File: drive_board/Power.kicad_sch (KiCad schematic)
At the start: 9 parts, among them J1 Molex_Megafit_02

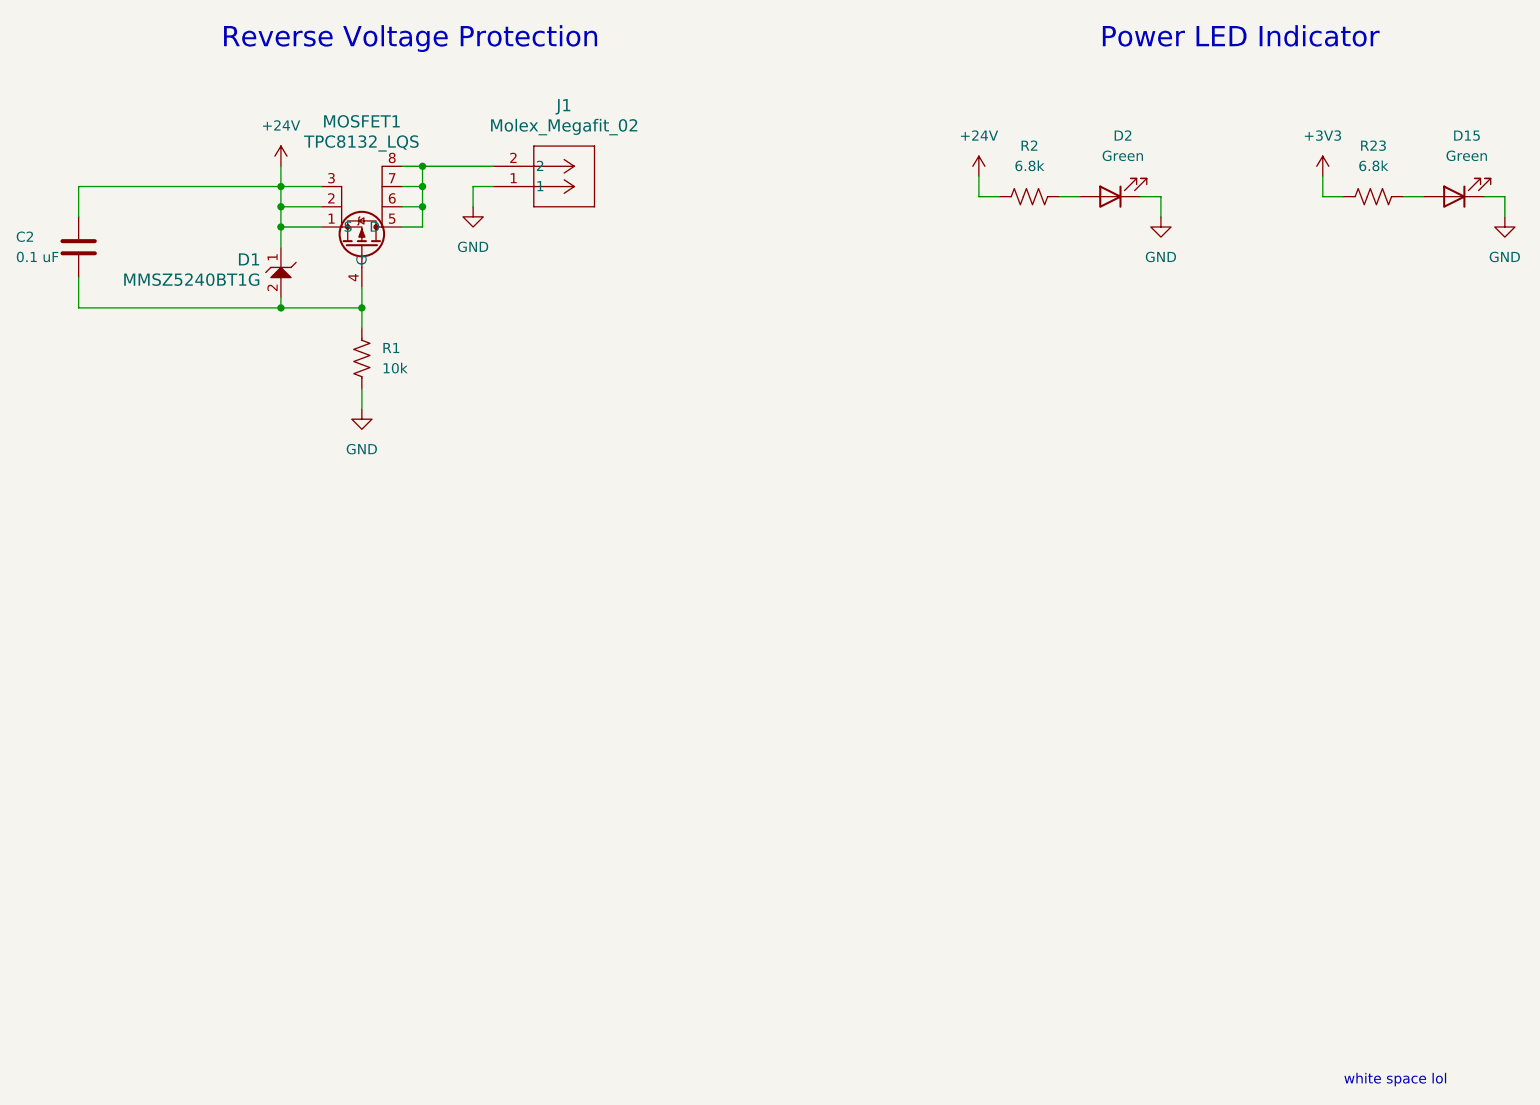
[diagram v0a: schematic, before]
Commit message: Change Testing Control Scheme
- Removed testing D-pad.
- Removed rotary encoder.
- Added two complete (maybe) joystick potentiometer circuits.
- Added dip switch (no circuit).
- Assigned some footprints.
- Grounded mounting holes.
- Added CAN transceiver terminating resistor (footprint only).
- Other stuff I prob forgot.
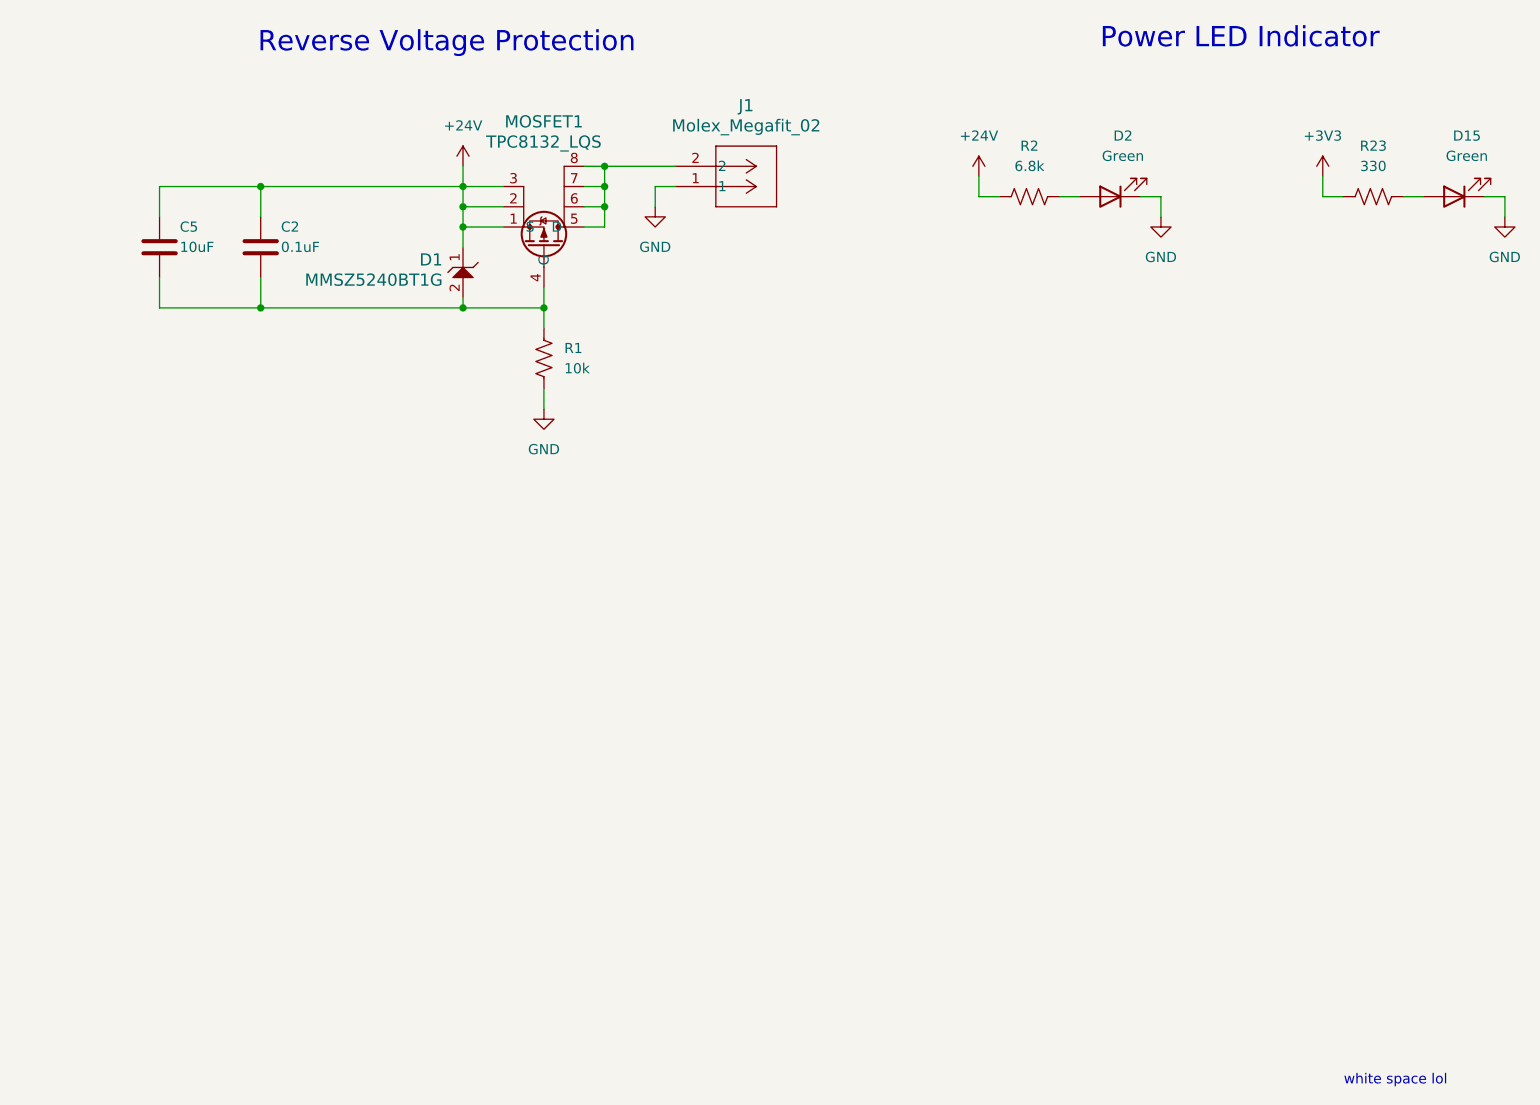
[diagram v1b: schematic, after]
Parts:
- added C5: 10uF, symbol Device:C
- C2: value 0.1 uF -> 0.1uF
- D15, D2: footprint (none) -> LED_SMD:LED_0603_1608Metric_Pad1.05x0.95mm_HandSolder
- R1, R2: footprint (none) -> Resistor_SMD:R_0603_1608Metric_Pad0.98x0.95mm_HandSolder
- R23: value 6.8k -> 330; footprint (none) -> Resistor_SMD:R_0603_1608Metric_Pad0.98x0.95mm_HandSolder
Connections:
- net +24V: now also C5.1
- net at C2.2, D1.2, MOSFET1.4 (G)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: now also C5.2
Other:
- moved on the sheet: C2, D1, J1, MOSFET1, R1

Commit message: Finish Schematic
- Assigned all footprints
- Added dipswitch and connected to RoveNode
- Updated PCB from schematic
- Added absolute encoder pins and connected to RoveNode
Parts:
- C2, C5: footprint (none) -> Capacitor_SMD:C_0603_1608Metric_Pad1.08x0.95mm_HandSolder

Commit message: Finish first draft
B approved
Did everything
Made room for traces
Placed everything in places
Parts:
- J1: footprint MRDT_Connectors:MOLEX_MegaFit_02_Horizontal -> megafit:CONN_SD-768290002_02_MOL
